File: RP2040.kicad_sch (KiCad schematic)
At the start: 27 parts, among them J1 USB_B_Micro, J2 Conn_01x02, U1 AMS1117-3.3, U5 W25Q128JVS, U6 RP2040, Y1 X322512MSB4SI

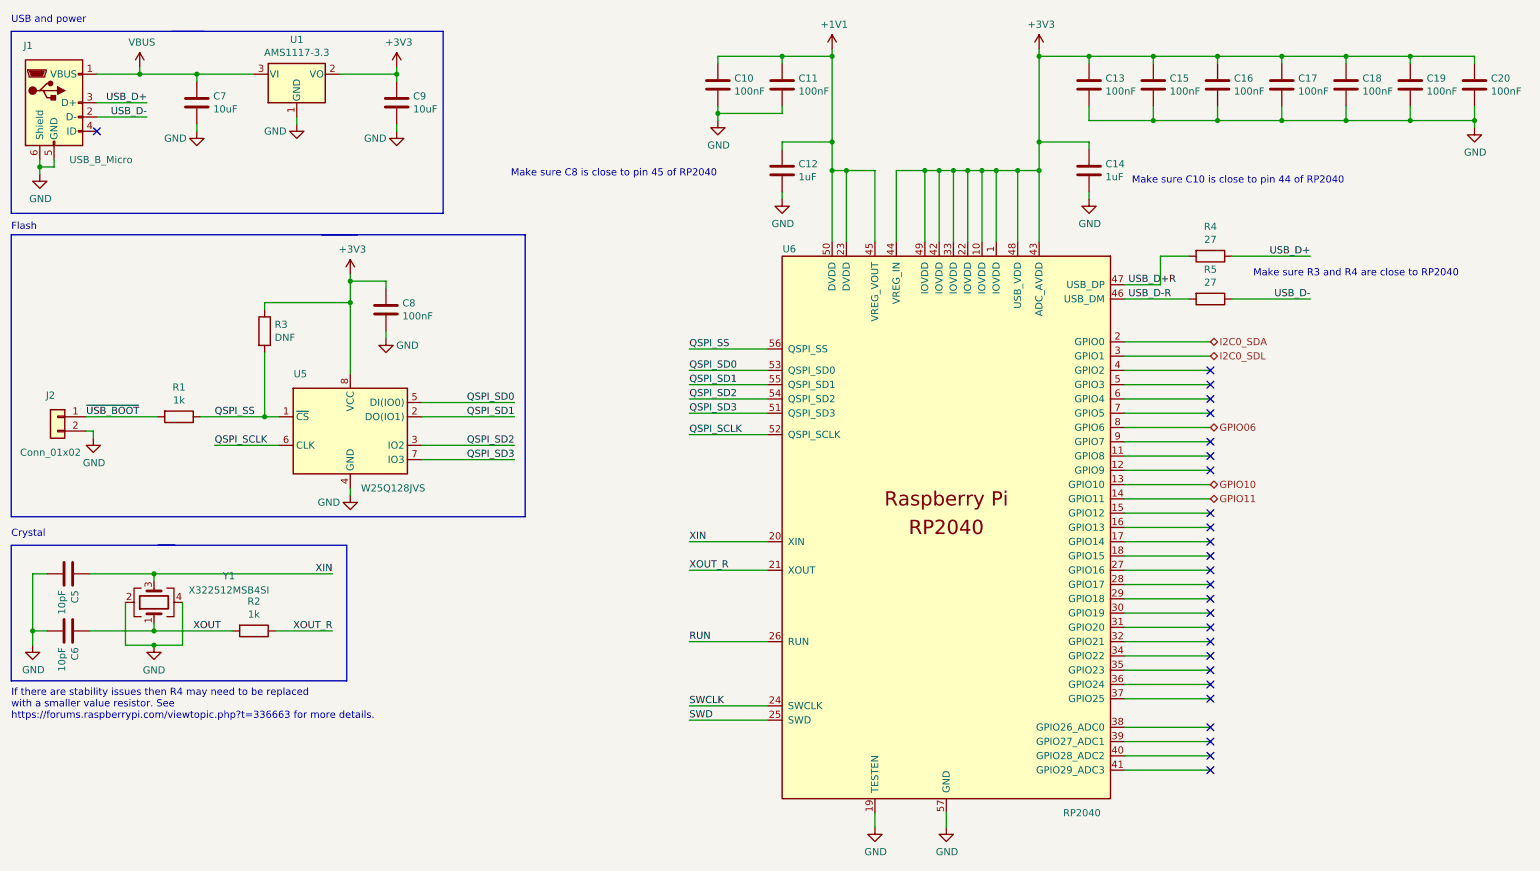
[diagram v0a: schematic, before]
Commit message: Keyboard driver (#25)
* Lots of pre-work before replacing RP2040 layout

* New RP2040 layout added

* FULLY ROUTED

* Clean up schematic

* More trace cleanup

* Final trace cleanup

Co-authored-by: Neil Enns <{ID}+{username}@users.noreply.github.com>
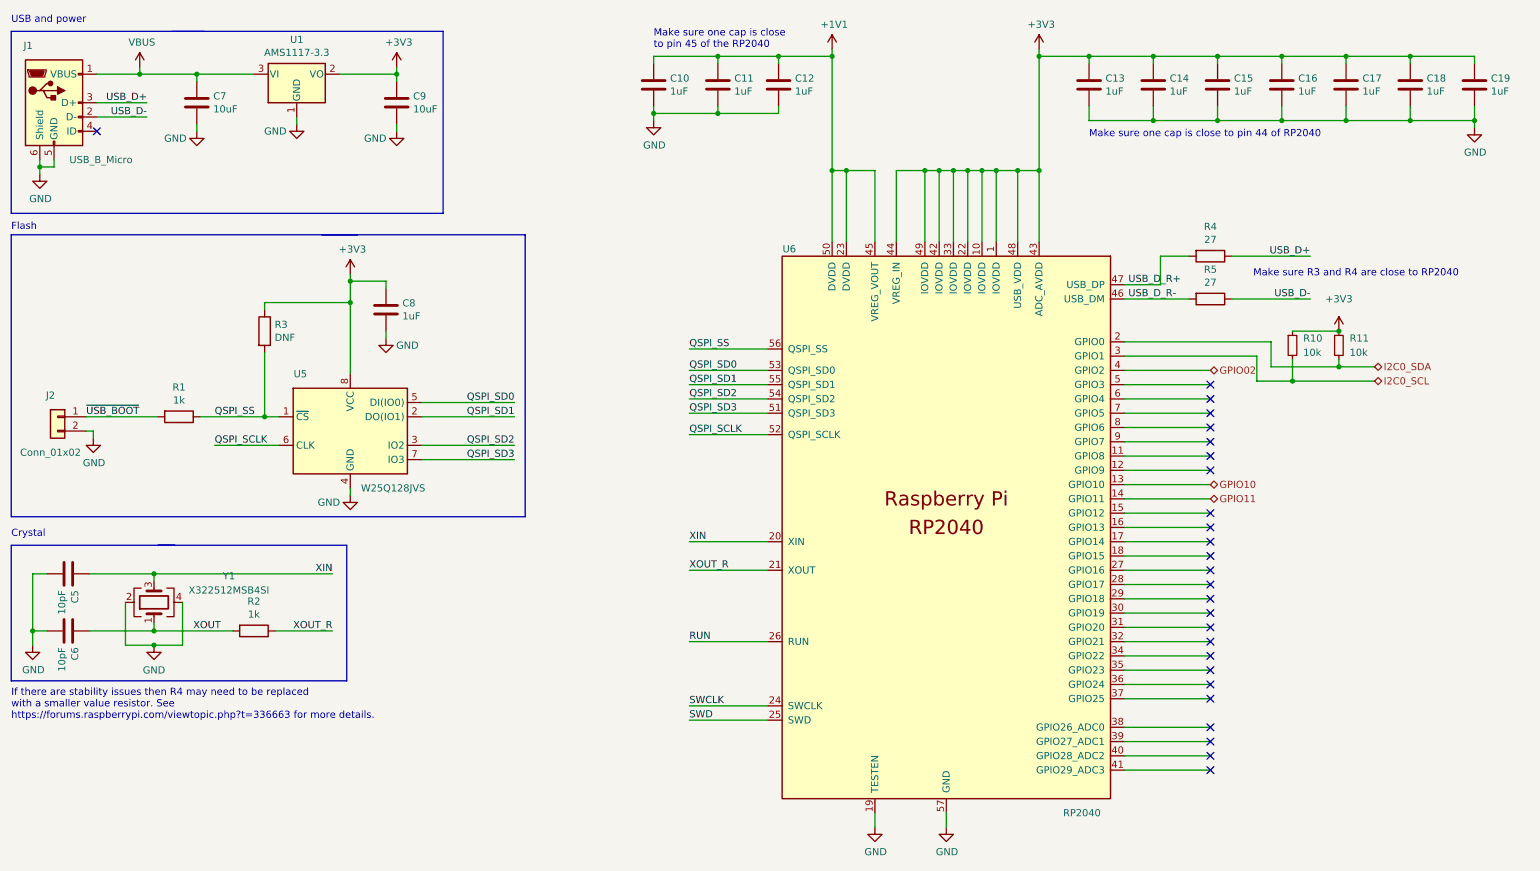
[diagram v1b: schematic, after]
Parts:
- removed C14: 1uF, Collins-FMS-3000:Perfect_0402, symbol Device:C
- added R10, R11: 10k, Resistor_SMD:R_1206_3216Metric_Pad1.30x1.75mm_HandSolder, symbol Device:R_Small
- C10, C11, C13, C8: value 100nF -> 1uF; footprint Collins-FMS-3000:Perfect_0402 -> Custom_Footprints:Perfect_0402; LCSC C1525 -> (none); MPN - JLCPCB (none) -> C52923
- C12: footprint Collins-FMS-3000:Perfect_0402 -> Custom_Footprints:Perfect_0402; LCSC C52923 -> (none); MPN - JLCPCB (none) -> C52923
- C14: renamed from C15; value 100nF -> 1uF; footprint Collins-FMS-3000:Perfect_0402 -> Custom_Footprints:Perfect_0402; LCSC C1525 -> (none); MPN - JLCPCB (none) -> C52923
- C15: renamed from C16; value 100nF -> 1uF; footprint Collins-FMS-3000:Perfect_0402 -> Custom_Footprints:Perfect_0402; LCSC C1525 -> (none); MPN - JLCPCB (none) -> C52923
- C16: renamed from C17; value 100nF -> 1uF; footprint Collins-FMS-3000:Perfect_0402 -> Custom_Footprints:Perfect_0402; LCSC C1525 -> (none); MPN - JLCPCB (none) -> C52923
- C17: renamed from C18; value 100nF -> 1uF; footprint Collins-FMS-3000:Perfect_0402 -> Custom_Footprints:Perfect_0402; LCSC C1525 -> (none); MPN - JLCPCB (none) -> C52923
- C18: renamed from C19; value 100nF -> 1uF; footprint Collins-FMS-3000:Perfect_0402 -> Custom_Footprints:Perfect_0402; LCSC C1525 -> (none); MPN - JLCPCB (none) -> C52923
- C19: renamed from C20; value 100nF -> 1uF; footprint Collins-FMS-3000:Perfect_0402 -> Custom_Footprints:Perfect_0402; LCSC C1525 -> (none); MPN - JLCPCB (none) -> C52923
- C5, C6: footprint Collins-FMS-3000:Perfect_0402 -> Custom_Footprints:Perfect_0402; LCSC C32949 -> (none); MPN - JLCPCB (none) -> C32949
- C7, C9: LCSC C19702 -> (none); MPN - JLCPCB (none) -> C19702
- R1, R2: footprint Collins-FMS-3000:Perfect_0402 -> Custom_Footprints:Perfect_0402; LCSC C11702 -> (none); MPN - JLCPCB (none) -> C11702
- R4, R5: LCSC C25190 -> (none); MPN - JLCPCB (none) -> C25190
- U1: LCSC C6186 -> (none); MPN - JLCPCB (none) -> C6186
- U5: LCSC C97521 -> (none); MPN - JLCPCB (none) -> C97521
- U6: footprint RP2040_minimal:RP2040-QFN-56 -> Custom_Footprints:QFN56P40_700X700X90L40X18T310N; LCSC C2040 -> (none); MPN - JLCPCB (none) -> C2040
- Y1: LCSC C9002 -> (none); MPN - JLCPCB (none) -> C9002
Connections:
- net +3V3: now also R10.1, R11.1
- net I2C0_SDA: now also R11.2
- net GPIO02: now reaches U6.4 (GPIO2)
- net GPIO06: no longer names the net of U6.8 (GPIO6)
- net I2C0_SDL renamed I2C0_SCL
- net I2C0_SCL: now also R10.2
- net USB_D+R renamed USB_D_R+
- net USB_D-R renamed USB_D_R-
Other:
- note added: "Make sure one cap is close to pin 44 of RP2040"
- note added: "Make sure one cap is close to pin 45 of the RP2040"
- note removed: "Make sure C10 is close to pin 44 of RP2040"
- note removed: "Make sure C8 is close to pin 45 of RP2040"
- moved on the sheet: C10, C11, C12
